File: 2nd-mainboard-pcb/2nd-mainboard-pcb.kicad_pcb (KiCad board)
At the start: 4 copper layers, 99 x 97.5 mm, 131 parts, among them J1 PJ-082BH, J10 Servo Motor BL Touch, J11 T3, J12 Steckverbinder_Male_Fans, J13 Steckverbinder_Female_Leistung, J14 FAN3, J15 Steckverbinder_Female_Motoren, J16 ISP, J18 Quartz, J19 T2, J2 Fan_12/5V_Regelung, J20 T2, J21 T2, J22 T3, J23 Conn_01x04_Socket, J24 Steckverbinder_Male_Leistung, J3 Fan_12/5V_Regelung, J4 FAN0, J5 FAN1, J6 FAN2, J7 Stepper Motor, J8 Servo Motor SM, J9 Microstepping, P1 USB_C_Receptacle_USB2.0_14P, SW3 PTS820 J25K SMTR LFS, U1 SQJ409EP-T1_GE3, U10 ATmega328PB-A, U12 MPU-6050, U2 SZ1SMB5927BT3G, U3 TPS56837HRPAR, U4 TPS565208, U5 FT232RL, U7 TPM16050-S6TR, U8 RJK0456DPB-00-J5, U9 RJK0456DPB-00-J5, Y1 ECS-160-18-4X-CKM

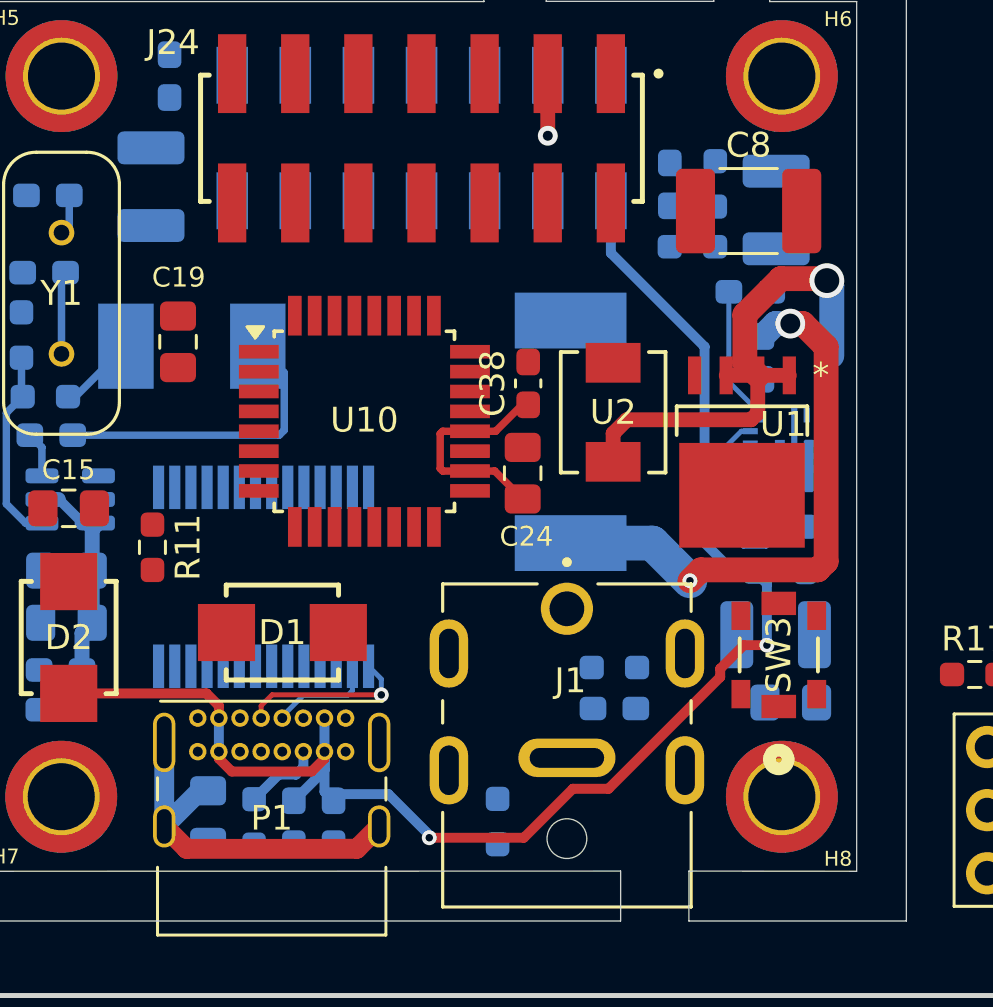
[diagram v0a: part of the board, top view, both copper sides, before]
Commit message: updated conns
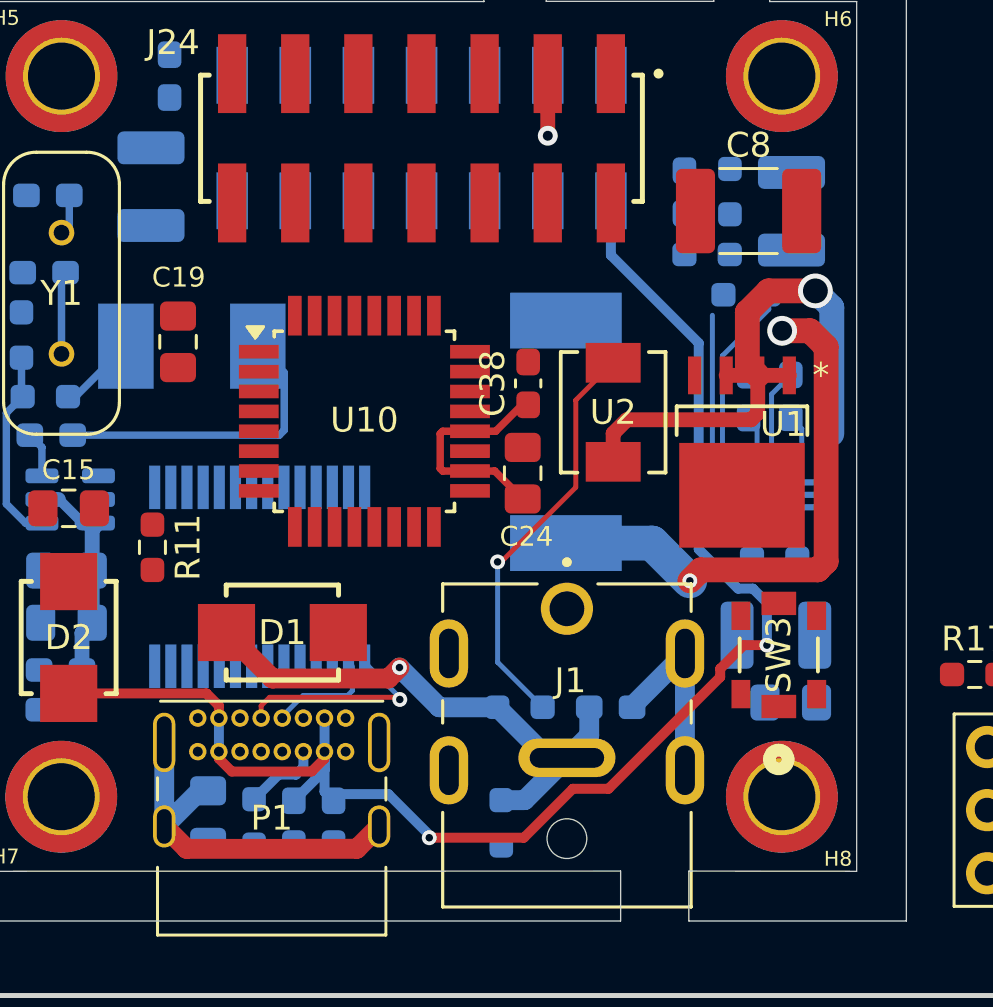
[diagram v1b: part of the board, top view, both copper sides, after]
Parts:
- moved R2 10.2 mm to (133.1, 121.8), turned to 0 degrees
- moved C9 4.22 mm to (133.2, 125.9), turned to 90 degrees
- moved R1 4.12 mm to (124.0, 138.4)
- moved C1 1.92 mm to (134.8, 125.9)
- moved U3 1.61 mm to (134.2, 129.6)
- moved R5 1.29 mm to (134.2, 132.4), turned to 0 degrees
- moved C2 0.67 mm to (130.6, 117.7)
- moved R3 0.67 mm to (132.4, 117.7)
- moved R4 0.67 mm to (131.5, 120.2), turned to 180 degrees
- moved C5 0.62 mm to (134.9, 118.4)
- moved L1 0.19 mm to (125.8, 127.3)
- moved R6 0.16 mm to (123.2, 143.1)
- moved C7 0.16 mm to (127.6, 138.4)
- moved U5 0.16 mm to (113.5, 133.2)
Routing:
- net GND2: track 0.00 -> 21.9 mm, vias 0 -> 1
- net Net-(U1-G): track 0.00 -> 16.6 mm, vias 0 -> 1
- net GND3: track 0.00 -> 7.75 mm
- net Net-(U3-SS): track 5.51 -> 1.97 mm
- net Net-(U3-PG): track 4.94 -> 8.02 mm
- net Net-(U3-SW): track 23.0 -> 25.6 mm
- net PWR_IN_PROT: track 21.1 -> 23.2 mm
- net Net-(U3-BOOT): track 0.00 -> 2.02 mm
- net Net-(U3-MODE): track 0.00 -> 1.41 mm
- net USBD+: track 6.88 -> 8.11 mm

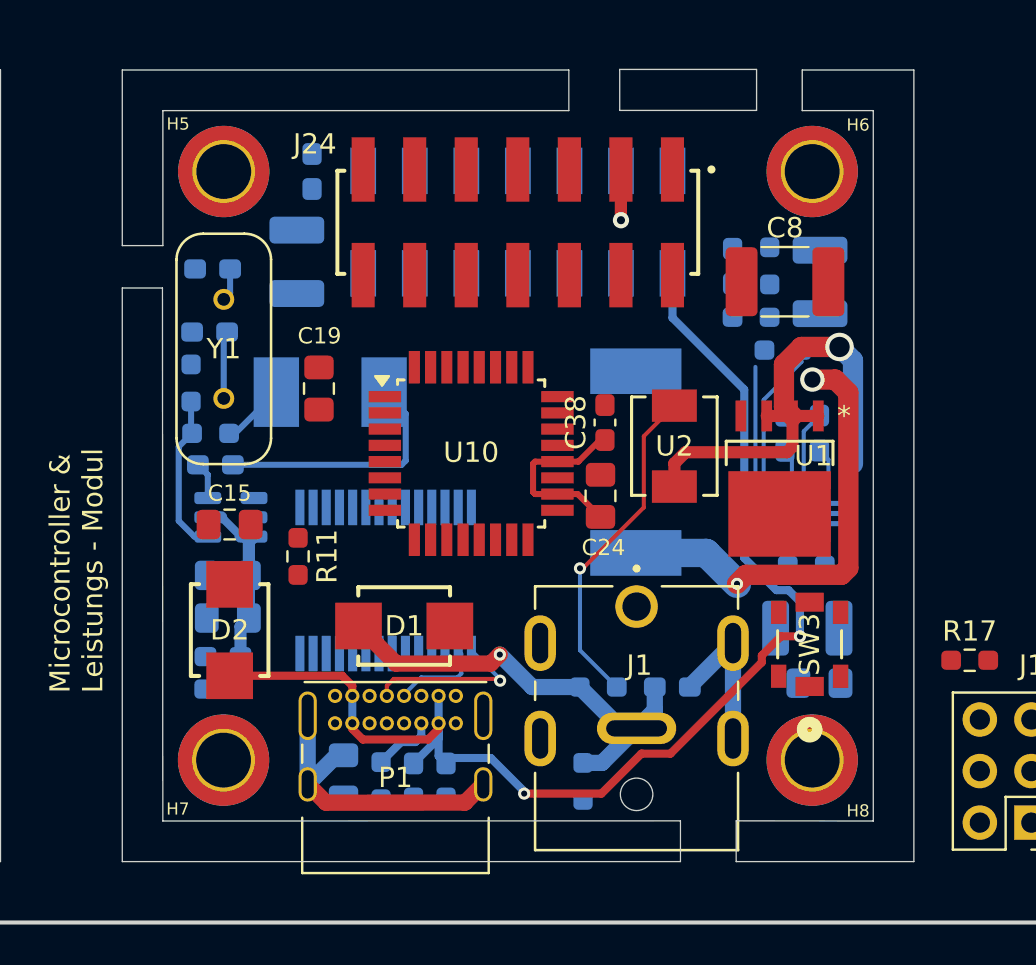
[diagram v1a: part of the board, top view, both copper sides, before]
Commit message: finished pcb design on main segment
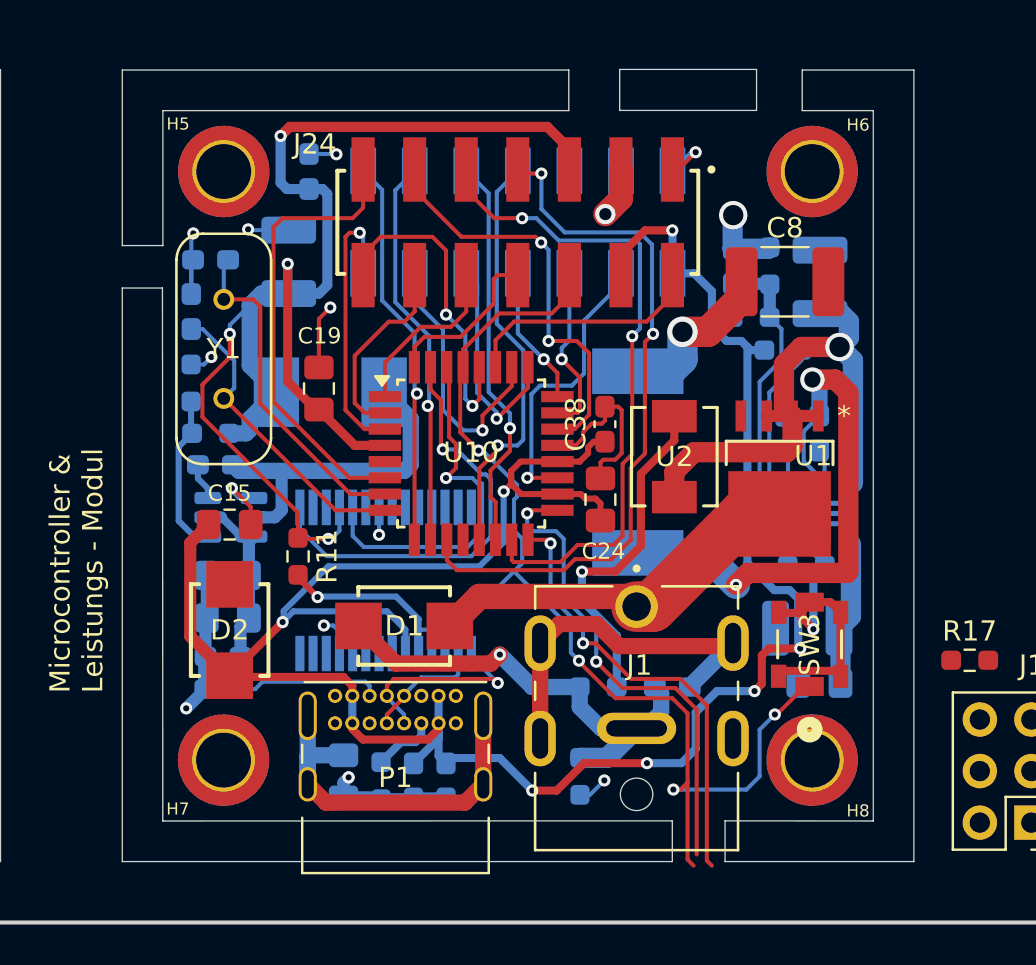
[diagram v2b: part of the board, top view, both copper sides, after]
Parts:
- moved C21 1.35 mm to (103.9, 119.9), turned to 90 degrees
- moved U2 0.52 mm to (127.7, 127.0)
- moved C22 0.46 mm to (104.8, 117.3)
- moved C14 0.40 mm to (108.7, 117.5)
- moved R6 0.29 mm to (123.0, 142.8)
- moved C24 0.18 mm to (124.1, 129.2)
- moved C20 0.15 mm to (109.7, 113.0)
- moved L1 0.10 mm to (125.9, 127.3)
- moved C38 0.08 mm to (124.3, 125.5)
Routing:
- net RESET: track 0.00 -> 66.5 mm, vias 0 -> 5
- net +5V_POW: track 3.17 -> 68.9 mm, vias 0 -> 4
- net GND: track 8.26 -> 68.2 mm, vias 0 -> 13
- net AREF: track 71.1 -> 120.2 mm, vias 2 -> 7
- net STEP: track 0.00 -> 35.1 mm, vias 0 -> 2
- net MOSI: track 0.00 -> 32.4 mm, vias 0 -> 2
- net SCK: track 0.00 -> 24.0 mm, vias 0 -> 2
- net LED_MOT0: track 0.00 -> 22.3 mm
- net MISO: track 0.00 -> 22.1 mm, vias 0 -> 2
- net TXD: track 0.00 -> 21.5 mm, vias 0 -> 1
- net FAN_01_PWM_clockwise: track 0.00 -> 20.6 mm, vias 0 -> 1
- net LED_MOT1: track 0.00 -> 20.5 mm, vias 0 -> 2
- net FAN_01_PWM_counterclockwise: track 0.00 -> 19.6 mm, vias 0 -> 1
- net FAN_3_PWM: track 0.00 -> 19.3 mm, vias 0 -> 1
- net FAN_2_PWM: track 0.00 -> 19.3 mm, vias 0 -> 1
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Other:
- outline, holes or cut-outs redrawn

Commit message: diplomarbeitsbesprechungabgeschlossen
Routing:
- net PWR_IN_PROT: track 34.6 -> 24.8 mm
- net +5V_POW: track 68.9 -> 73.5 mm, vias 4 -> 5
- net +12V: track 23.1 -> 27.5 mm, vias 3 -> 4

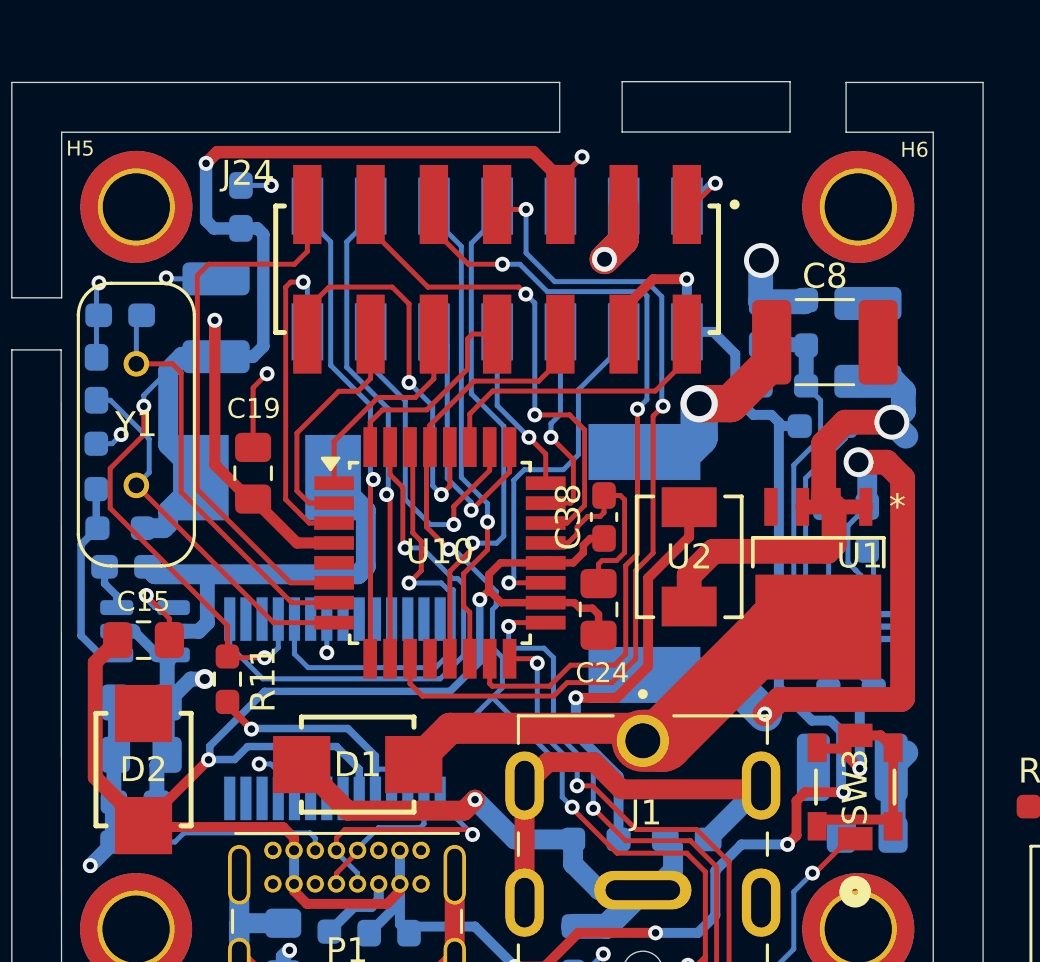
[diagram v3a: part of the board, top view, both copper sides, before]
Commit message: stacked design verbessert, power plane aufgeteilt
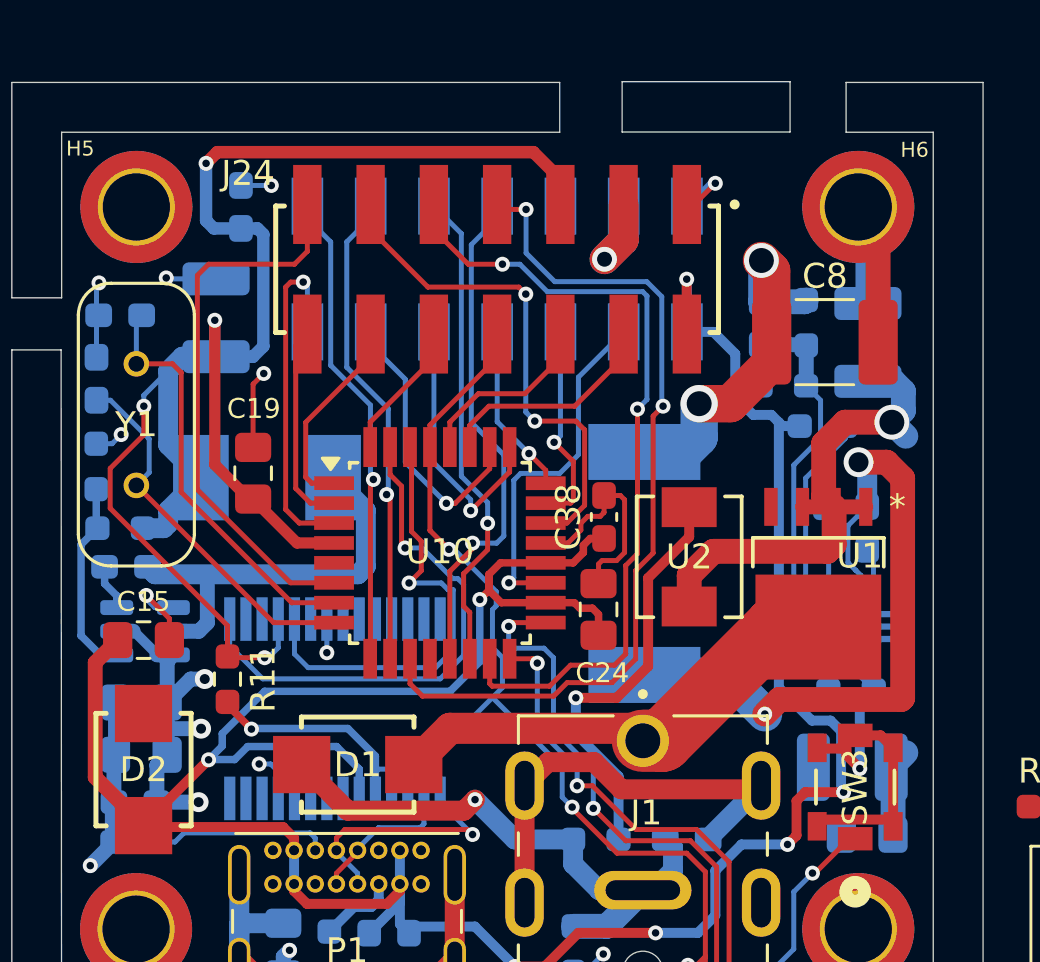
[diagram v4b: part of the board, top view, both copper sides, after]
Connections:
- J15 pad 02: SDA -> AREF
- J15 pad 04: AREF -> SDA
- J15 pad 06: RESET -> SCL
- J15 pad 08: DIR -> RESET
- J15 pad 10: BLT_Servo -> DIR
- J15 pad 12: BLT_Switch -> BLT_Servo
- J15 pad 14: SCL -> BLT_Switch
- J24 pad 02: SDA -> AREF
- J24 pad 04: AREF -> SDA
- J24 pad 06: RESET -> SCL
- J24 pad 08: DIR -> RESET
- J24 pad 10: BLT_Servo -> DIR
- J24 pad 12: BLT_Switch -> BLT_Servo
- J24 pad 14: SCL -> BLT_Switch
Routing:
- net GND: track 68.1 -> 77.8 mm
- net SCL: track 16.0 -> 7.47 mm, vias 2 -> 0
- net +12V: track 27.5 -> 34.0 mm, vias 4 -> 6
- net +5V_POW: track 73.5 -> 69.9 mm, vias 5 -> 4
- net SDA: track 12.0 -> 9.11 mm
- net RESET: track 66.5 -> 63.8 mm
- net DIR: track 8.27 -> 5.60 mm
- net ADC3: track 13.4 -> 11.3 mm
- net AREF: track 120.2 -> 118.4 mm
- net BLT_Switch: track 9.67 -> 8.17 mm

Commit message: more layout
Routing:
- net PWR_IN_PROT: track 24.8 -> 32.2 mm
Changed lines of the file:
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@@
 	)
 	(segment
-		(start 118.089103 121.642625)
-		(end 119.231728 120.5)
+		(start 118.089103 121.651761)
+		(end 119.240864 120.5)
 		(width 0.2)
 		(layer "F.Cu")
@@
 	)
 	(segment
-		(start 118.089103 122.642625)
-		(end 118.089103 121.642625)
+		(start 121.1 120.5)
+		(end 122.526603 119.073397)
 		(width 0.2)
 		(layer "F.Cu")
@@
 	)
 	(segment
-		(start 121.1 120.5)
-		(end 122.526603 119.073397)
+		(start 119.240864 120.5)
+		(end 121.1 120.5)
 		(width 0.2)
 		(layer "F.Cu")
@@
 	)
 	(segment
-		(start 119.231728 120.5)
-		(end 121.1 120.5)
+		(start 118.089103 122.642625)
+		(end 118.089103 121.651761)
 		(width 0.2)
 		(layer "F.Cu")
@@
 	)
 	(segment
+		(start 117.289103 122.642625)
+		(end 117.289103 121.760897)
+		(width 0.2)
+		(layer "F.Cu")
+		(net 29)
+	)
+	(segment
 		(start 124.801471 138.95)
 		(end 127.6 138.95)
@@
 	)
 	(segment
-		(start 117.289103 122.642625)
-		(end 117.289103 125.989103)
+		(start 117.289103 121.760897)
+		(end 119.986603 119.063397)
 		(width 0.2)
 		(layer "F.Cu")
@@
 	)
 	(segment
-		(start 119.986603 119.063397)
-		(end 119.986603 118.105113)
+		(start 117.289103 122.642625)
+		(end 117.289103 125.989103)
 		(width 0.2)
 		(layer "F.Cu")
@@
 	)
 	(segment
-		(start 117.289103 121.760897)
-		(end 119.986603 119.063397)
-		(width 0.2)
-		(layer "F.Cu")
-		(net 29)
-	)
-	(segment
 		(start 123 137.148529)
 		(end 124.801471 138.95)
@@
 	)
 	(segment
-		(start 117.289103 122.642625)
-		(end 117.289103 121.760897)
-		(width 0.2)
-		(layer "F.Cu")
-		(net 29)
-	)
-	(segment
 		(start 127.6 138.95)
 		(end 128.35 139.7)
@@
 	)
 	(segment
+		(start 119.986603 119.063397)
+		(end 119.986603 118.105113)
+		(width 0.2)
+		(layer "F.Cu")
+		(net 29)
+	)
+	(segment
 		(start 128.65 147.2)
 		(end 128.35 146.9)
@@
 	)
 	(segment
+		(start 135.838022 121.644665)
+		(end 136.5 122.306643)
+		(width 1)
+		(layer "B.Cu")
+		(net 58)
+	)
+	(segment
 		(start 136.3 121.182687)
 		(end 136.3 120.4)
@@
 	)
 	(segment
+		(start 136.5 122.306643)
+		(end 136.5 128.703629)
+		(width 1)
+		(layer "B.Cu")
+		(net 58)
+	)
+	(segment
 		(start 135.838022 121.644665)
 		(end 136.3 121.182687)
@@
 	)
 	(segment
-		(start 123.5 124.984314)
-		(end 123.5 121.951471)
-		(width 0.2)
-		(layer "F.Cu")
-		(net 100)
-	)
-	(segment
 		(start 114.906603 112.900113)
 		(end 114.906603 113.917613)
@@
 	)
 	(segment
-		(start 120.856617 116.217613)
-		(end 121.138315 116.499311)
+		(start 123.5 124.984314)
+		(end 122.791689 125.692625)
 		(width 0.2)
 		(layer "F.Cu")
@@
 	)
 	(segment
-		(start 121.939103 125.692625)
-		(end 122.791689 125.692625)
+		(start 120.856617 116.217613)
+		(end 121.138315 116.499311)
 		(width 0.2)
 		(layer "F.Cu")
@@
 	)
 	(segment
-		(start 123.148525 121.599996)
-		(end 121.5 121.599996)
+		(start 123.5 122.826468)
+		(end 123.5 124.984314)
 		(width 0.2)
 		(layer "F.Cu")
@@
 	(segment
 		(start 122.791689 125.692625)
-		(end 123.5 124.984314)
+		(end 121.939103 125.692625)
 		(width 0.2)
 		(layer "F.Cu")
@@
 	)
 	(segment
-		(start 123.5 121.951471)
-		(end 123.148525 121.599996)
+		(start 121.65 121.85)
+		(end 122.523532 121.85)
+		(width 0.2)
+		(layer "F.Cu")
+		(net 100)
+	)
+	(segment
+		(start 121.5 122)
+		(end 121.65 121.85)
+		(width 0.2)
+		(layer "F.Cu")
+		(net 100)
+	)
+	(segment
+		(start 122.523532 121.85)
+		(end 123.5 122.826468)
 		(width 0.2)
 		(layer "F.Cu")
@@
 	)
 	(via
-		(at 121.5 121.599996)
+		(at 121.5 122)
 		(size 0.6)
 		(drill 0.3)
@@
 	)
 	(segment
-		(start 121.138315 121.238311)
-		(end 121.5 121.599996)
+		(start 121.5 122)
+		(end 121.138315 121.638315)
 		(width 0.2)
 		(layer "B.Cu")
@@
 	)
 	(segment
-		(start 121.138315 116.499311)
-		(end 121.138315 121.238311)
+		(start 121.138315 121.638315)
+		(end 121.138315 116.499311)
 		(width 0.2)
 		(layer "B.Cu")
@@
 		(min_thickness 0.25)
 		(filled_areas_thickness no)
-		(fill
+		(fill yes
 			(thermal_gap 0.5)
 			(thermal_bridge_width 0.5)
@@
 		(min_thickness 0.25)
 		(filled_areas_thickness no)
-		(fill
+		(fill yes
 			(thermal_gap 0.5)
 			(thermal_bridge_width 0.5)
@@
 		(min_thickness 0.25)
 		(filled_areas_thickness no)
-		(fill
+		(fill yes
 			(thermal_gap 0.5)
 			(thermal_bridge_width 0.5)
